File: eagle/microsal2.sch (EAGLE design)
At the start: 68 parts, among them IC20 4023N, IC26 4001N, IC27 74LS373N, IC28 74LS32N, IC29 74LS05N, IC30 4029N, IC31 4013N, IC32 4023N, IC33 4069N, IC34 74LS02N, IC35 74LS373N, IC36 74LS373N, IC37 74LS05N, IC38 74LS05N, IC39 4069N, IC40 4069N, IC41 4503N, IC42 74LS74N, IC43 74LS05N, IC44 4503N, IC45 74LS05N, IC46 4503N, IC48 74LS02N, IC49 74LS139N, IC50 74LS32N, IC51 74LS05N, IC52 74LS05N, IC53 74LS153N, IC54 1489N, IC55 1489N, IC56 74LS32N, IC57 1488N, IC58 1488N, IC59 74LS74N, IC60 74LS05N

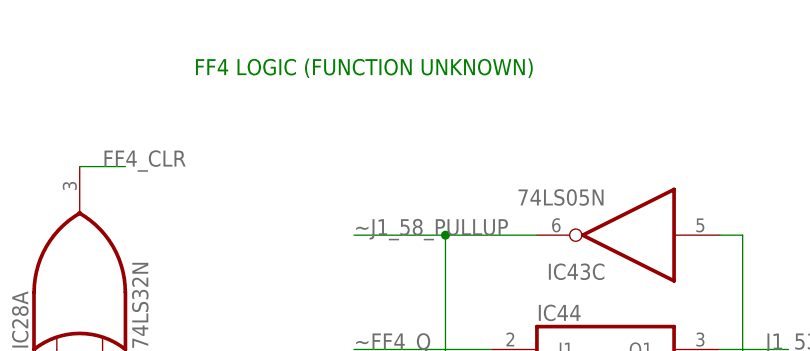
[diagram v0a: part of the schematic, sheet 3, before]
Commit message: Reverse engineered RAM board, full ROM dump/analysis
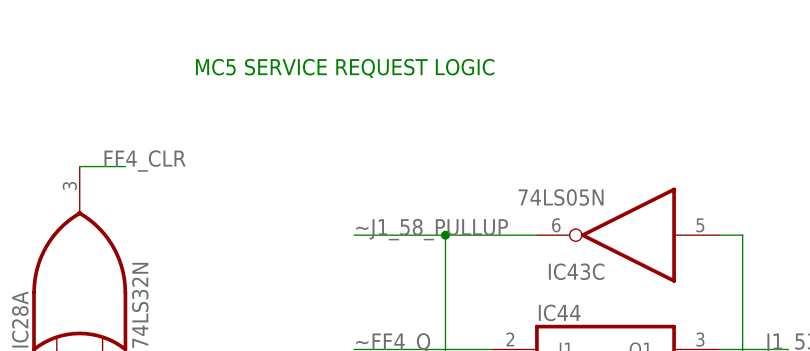
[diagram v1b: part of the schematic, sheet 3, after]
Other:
- note added: "MC5 SERVICE REQUEST LOGIC"
- note removed: "FF4 LOGIC (FUNCTION UNKNOWN)"
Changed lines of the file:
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@@
 <?xml version="1.0" encoding="utf-8"?>
 <!DOCTYPE eagle SYSTEM "eagle.dtd">
-<eagle version="8.2.2">
+<eagle version="9.0.0">
 <drawing>
 <settings>
 <setting alwaysvectorfont="no"/>
+<setting keepoldvectorfont="yes"/>
 <setting verticaltext="up"/>
 </settings>
-<grid distance="0.1" unitdist="inch" unit="inch" style="lines" multiple="1" display="no" altdistance="0.05" altunitdist="inch" altunit="inch"/>
+<grid distance="0.1" unitdist="inch" unit="inch" style="lines" multiple="1" display="no" altdistance="0.01" altunitdist="inch" altunit="inch"/>
 <layers>
 <layer number="1" name="Top" color="4" fill="1" visible="no" active="no"/>
@@
 <sheet>
 <plain>
-<text x="198.12" y="205.74" size="1.778" layer="91">FF4 LOGIC (FUNCTION UNKNOWN)</text>
+<text x="198.12" y="205.74" size="1.778" layer="91">MC5 SERVICE REQUEST LOGIC</text>
 <text x="66.04" y="205.74" size="1.778" layer="91">EXTERNAL BUS OUTPUT LOGIC</text>
 <frame x1="0" y1="0" x2="279.4" y2="215.9" columns="8" rows="5" layer="91"/>
@@
 <compatibility>
 <note version="8.2" severity="warning">
-Since Version 8.2, Eagle supports online libraries. The ids
+Since Version 8.2, EAGLE supports online libraries. The ids
 of those online libraries will not be understood (or retained)
 with this version.
